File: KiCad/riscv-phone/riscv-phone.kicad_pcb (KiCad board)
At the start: 2 copper layers, 0 parts

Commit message: Initial microcontroller board
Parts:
- added C10: 12pF, Capacitor_SMD:C_0603_1608Metric, F.Cu at (134.7, 133.0)
- added C11: 0.1uF, Capacitor_SMD:C_0603_1608Metric, F.Cu at (128.8, 141.2)
- added C12: 0.1uF, Capacitor_SMD:C_0603_1608Metric, F.Cu at (144.1, 139.3)
- added C13: 0.1uF, Capacitor_SMD:C_0603_1608Metric, F.Cu at (138.2, 150.6)
- added C14: 0.1uF, Capacitor_SMD:C_0603_1608Metric, F.Cu at (135.6, 136.4)
- added C15: 0.1uF, Capacitor_SMD:C_0603_1608Metric, F.Cu at (146.3, 140.0)
- added C16: 1uF, Capacitor_SMD:C_0603_1608Metric, F.Cu at (141.9, 150.5)
- added C17: 1uF, Capacitor_SMD:C_0603_1608Metric, F.Cu at (132.8, 146.3)
- added C18: 0.1uF, Capacitor_SMD:C_0603_1608Metric, F.Cu at (126.7, 143.8)
- added C19: 0.1uF, Capacitor_SMD:C_0603_1608Metric, F.Cu at (143.1, 130.8)
- added C20: 1uF, Capacitor_SMD:C_0603_1608Metric, F.Cu at (143.1, 132.5)
- added C21: 0.1uF, Capacitor_SMD:C_0603_1608Metric, F.Cu at (157.2, 134.2)
- added C22: 0.1uF, Capacitor_SMD:C_0603_1608Metric, F.Cu at (137.3, 111.9)
- added C23: 12pF, Capacitor_SMD:C_0603_1608Metric, F.Cu at (130.6, 112.5)
- added C24: 4.7uF, Capacitor_SMD:C_0603_1608Metric, F.Cu at (129.0, 121.8)
- added C25: 4.7uF, Capacitor_SMD:C_0603_1608Metric, B.Cu at (136.5, 120.9)
- added C26: 4.7uF, Capacitor_SMD:C_0603_1608Metric, B.Cu at (136.5, 117.3)
- added C27: 12pF, Capacitor_SMD:C_0603_1608Metric, F.Cu at (124.7, 112.5)
- added C28: 0.1uF, Capacitor_SMD:C_0603_1608Metric, F.Cu at (127.4, 121.8)
- added C29: 0.1uF, Capacitor_SMD:C_0603_1608Metric, B.Cu at (135.0, 120.9)
- added C30: 0.1uF, Capacitor_SMD:C_0603_1608Metric, B.Cu at (135.0, 117.3)
- added C31: 0.1uF, Capacitor_SMD:C_0603_1608Metric, F.Cu at (141.7, 126.7)
- added C32: 0.1uF, Capacitor_SMD:C_0603_1608Metric, F.Cu at (145.2, 117.3)
- added C33: 0.1uF, Capacitor_SMD:C_0603_1608Metric, F.Cu at (137.9, 126.7)
- added C34: 0.1uF, Capacitor_SMD:C_0603_1608Metric, F.Cu at (145.2, 122.2)
- added C35: 0.1uF, Capacitor_SMD:C_0603_1608Metric, F.Cu at (133.4, 111.1)
- added C36: 0.1uF, Capacitor_SMD:C_0603_1608Metric, F.Cu at (142.5, 110.9)
- added C59: 0.1uF, Capacitor_SMD:C_0603_1608Metric, F.Cu at (158.4, 150.2)
- added C7: 10nF, Capacitor_SMD:C_0603_1608Metric, F.Cu at (126.0, 132.1)
- added C8: 0.1uF, Capacitor_SMD:C_0603_1608Metric, F.Cu at (156.2, 130.6)
- added C9: 12pF, Capacitor_SMD:C_0603_1608Metric, F.Cu at (140.7, 131.7)
- added C90: 1uF, Capacitor_SMD:C_0603_1608Metric, B.Cu at (122.9, 123.7)
- added C91: 1uF, Capacitor_SMD:C_0603_1608Metric, B.Cu at (126.6, 123.6)
- added C92: 1uF, Capacitor_SMD:C_0603_1608Metric, B.Cu at (126.6, 129.2)
- added C93: 1uF, Capacitor_SMD:C_0603_1608Metric, B.Cu at (123.4, 129.2)
- added D1: 1N4448W, Diode_SMD:D_SOD-123, F.Cu at (121.3, 132.5)
- added D2: BAT54L, Package_TO_SOT_SMD:SOT-23, F.Cu at (125.9, 129.2)
- added D3: BAT54L, Package_TO_SOT_SMD:SOT-23, F.Cu at (121.4, 142.5)
- added D4: SLEEP_LED, LED_SMD:LED_0805_2012Metric, F.Cu at (125.9, 150.4)
- added D5: D_TVS, LED_SMD:LED_0603_1608Metric_Pad1.05x0.95mm_HandSolder, F.Cu at (120.5, 126.1)
- added D8: D_TVS, LED_SMD:LED_0603_1608Metric_Pad1.05x0.95mm_HandSolder, F.Cu at (124.8, 120.4)
- added D9: D_TVS, LED_SMD:LED_0603_1608Metric_Pad1.05x0.95mm_HandSolder, F.Cu at (124.8, 117.1)
- added FB1: 600R, Inductor_SMD:L_0805_2012Metric_Pad1.15x1.40mm_HandSolder, B.Cu at (138.4, 121.0)
- added FB2: 600R, Inductor_SMD:L_0805_2012Metric_Pad1.15x1.40mm_HandSolder, B.Cu at (138.4, 117.2)
- added J1: USB_B_Micro, Connector_USB:USB_Micro-B_Molex-105017-0001, F.Cu at (120.9, 119.1)
- added J2: Conn_01x04, Connector_PinHeader_2.54mm:PinHeader_1x04_P2.54mm_Vertical, F.Cu at (119.6, 153.9)
- added J3: Conn_01x04, Connector_PinHeader_2.54mm:PinHeader_1x04_P2.54mm_Vertical, F.Cu at (153.4, 116.1)
- added J4: Conn_01x06, Connector_PinHeader_2.54mm:PinHeader_1x06_P2.54mm_Vertical, F.Cu at (148.3, 111.8)
- added J5: Conn_01x04, Connector_PinHeader_2.54mm:PinHeader_1x04_P2.54mm_Vertical, F.Cu at (161.3, 121.2)
- added J6: Conn_01x06, Connector_PinHeader_2.54mm:PinHeader_1x06_P2.54mm_Vertical, F.Cu at (161.3, 152.4)
- added J7: Conn_01x09, Connector_PinHeader_2.54mm:PinHeader_1x09_P2.54mm_Vertical, F.Cu at (124.7, 154.1)
- added J8: Conn_01x02, Connector_PinHeader_2.54mm:PinHeader_1x02_P2.54mm_Vertical, F.Cu at (121.7, 111.1)
- added Q1: Q_DUAL_NMOS_S1G1D2S2G2D1, Package_TO_SOT_SMD:SOT-363_SC-70-6, F.Cu at (126.7, 136.4)
- added Q2: IRLML6402, Package_TO_SOT_SMD:SOT-23, F.Cu at (119.5, 138.9)
- added R10: 100k, Resistor_SMD:R_0603_1608Metric, F.Cu at (123.7, 139.1)
- added R11: 4.7k, Resistor_SMD:R_0603_1608Metric, F.Cu at (123.8, 150.2)
- added R12: 100, Resistor_SMD:R_0603_1608Metric, F.Cu at (145.9, 128.1)
- added R23: 12k, Resistor_SMD:R_0603_1608Metric, F.Cu at (127.6, 117.3)
- added R24: 12k, Resistor_SMD:R_0603_1608Metric, F.Cu at (126.7, 125.2)
- added R25: 4.7k, Resistor_SMD:R_0603_1608Metric, F.Cu at (147.6, 114.8)
- added R26: 10k, Resistor_SMD:R_0603_1608Metric, F.Cu at (145.0, 113.8)
- added R27: 1k, Resistor_SMD:R_0603_1608Metric, F.Cu at (133.9, 129.5)
- added R28: 1k, Resistor_SMD:R_0603_1608Metric, F.Cu at (147.4, 118.9)
- added R29: 1k, Resistor_SMD:R_0603_1608Metric, F.Cu at (132.3, 127.3)
- added R30: 1k, Resistor_SMD:R_0603_1608Metric, F.Cu at (149.9, 120.9)
- added R34: 2.2k, Resistor_SMD:R_0603_1608Metric, F.Cu at (148.0, 149.5)
- added R35: 2.2k, Resistor_SMD:R_0603_1608Metric, F.Cu at (146.3, 149.5)
- added R53: 100k, Resistor_SMD:R_0603_1608Metric, F.Cu at (156.2, 126.5)
- added R54: 4.7k, Resistor_SMD:R_0603_1608Metric, F.Cu at (158.2, 145.9)
- added R6: 100k, Resistor_SMD:R_0603_1608Metric, F.Cu at (121.3, 134.7)
- added R7: 100k, Resistor_SMD:R_0603_1608Metric, F.Cu at (124.2, 126.1)
- added R8: 100k, Resistor_SMD:R_0603_1608Metric, F.Cu at (124.2, 142.2)
- added R9: 100k, Resistor_SMD:R_0603_1608Metric, F.Cu at (123.7, 146.6)
- added RST1: Reset, Button_Switch_SMD:SW_SPST_B3U-1000P-B, F.Cu at (121.3, 129.0)
- added U1: FE310-G000, Package_DFN_QFN:QFN-48-1EP_6x6mm_P0.4mm_EP4.66x4.66mm_ThermalVias, F.Cu at (138.8, 142.4)
- added U12: SC18IS600, Package_SO:TSSOP-16_4.4x5mm_P0.65mm, F.Cu at (153.2, 146.1)
- added U17: 74AHC1G08, Package_TO_SOT_SMD:SOT-23-5, F.Cu at (129.7, 148.2)
- added U18: M95256-WMN6P, Package_SO:SOIC-8_3.9x4.9mm_P1.27mm, F.Cu at (153.4, 152.9)
- added U2: IL25LP128, Package_SO:SOIJ-8_5.3x5.3mm_P1.27mm, F.Cu at (152.4, 128.9)
- added U5: 74CBTLV3257, Package_SO:TSSOP-16_4.4x5mm_P0.65mm, F.Cu at (153.5, 138.0)
- added U9: FT2232H, Package_QFP:LQFP-64_10x10mm_P0.5mm, F.Cu at (137.5, 119.3)
- added U90: TLV75533PDBV, Package_TO_SOT_SMD:SOT-23-5, B.Cu at (126.6, 126.4)
- added U91: TLV75518PDBV, Package_TO_SOT_SMD:SOT-23-5, B.Cu at (122.8, 126.4)
- added X1: SiT1533, riscv-phone:Crystal_SMD_2012-4Pin_2.0x1.2mm, F.Cu at (129.3, 144.0)
- added Y1: 16 MHz, Crystal:Crystal_SMD_3225-4Pin_3.2x2.5mm, F.Cu at (137.7, 132.3)
- added Y2: 12 MHz, Crystal:Crystal_SMD_3225-4Pin_3.2x2.5mm, F.Cu at (127.6, 112.5)
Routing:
- net +1V8: track 0.00 -> 216.0 mm, vias 0 -> 10
- net /Microcontroller/VDD_3V3_MOFF: track 0.00 -> 187.9 mm, vias 0 -> 12
- net +3V3: track 0.00 -> 184.8 mm, vias 0 -> 8
- net GND: track 0.00 -> 177.1 mm, vias 0 -> 33
- net /Program and Debug/VUSB: track 0.00 -> 66.3 mm, vias 0 -> 3
- net /RESET: track 0.00 -> 59.1 mm, vias 0 -> 8
- net /Microcontroller/RESET_N_1V8: track 0.00 -> 45.3 mm, vias 0 -> 3
- net /Microcontroller/DEBUG_RX: track 0.00 -> 40.1 mm, vias 0 -> 2
- net /Microcontroller/KEYPAD_INT: track 0.00 -> 37.1 mm, vias 0 -> 1
- net /Microcontroller/MOSI: track 0.00 -> 36.8 mm, vias 0 -> 4
- net /Program and Debug/VCORE_FT: track 0.00 -> 35.9 mm
- net /Microcontroller/SCK: track 0.00 -> 33.3 mm, vias 0 -> 4
- net /Microcontroller/MISO: track 0.00 -> 32.5 mm, vias 0 -> 4
- net /Microcontroller/DEBUG_TX: track 0.00 -> 31.0 mm, vias 0 -> 2
- net /Microcontroller/QSPI_CS: track 0.00 -> 27.3 mm
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- added copper zone on B.Cu, net GND
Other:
- board outline added: 46.5 x 47 mm
- net class Default: clearance 0.2 -> 0.1524; trace_width 0.25 -> 0.1524; via_dia 0.8 -> 0.6858; via_drill 0.4 -> 0.3302
- rule trace_clearance: 0.2 -> 0.1524
- rule trace_min: 0.2 -> 0.1524
- rule via_min_drill: 0.3 -> 0.254
- rule via_min_size: 0.4 -> 0.6858

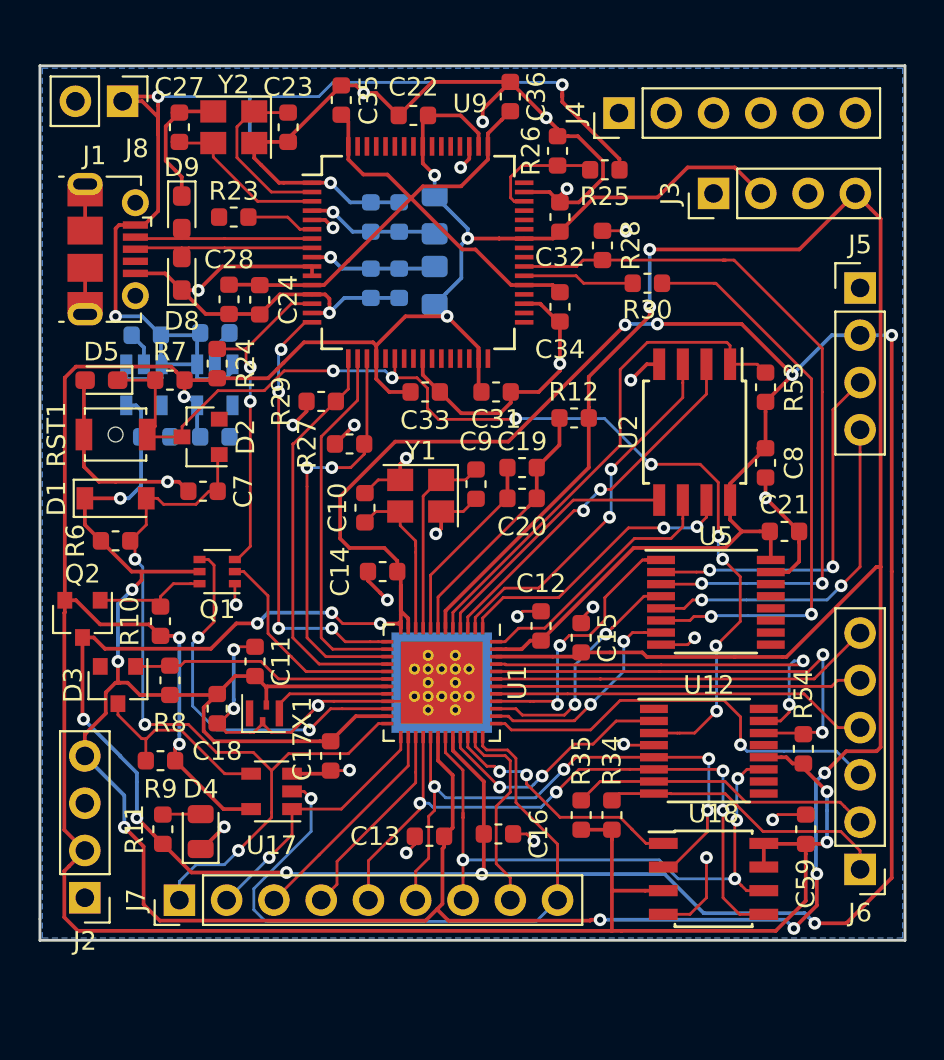
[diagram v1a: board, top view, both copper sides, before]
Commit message: added mounting holes, finalized layout
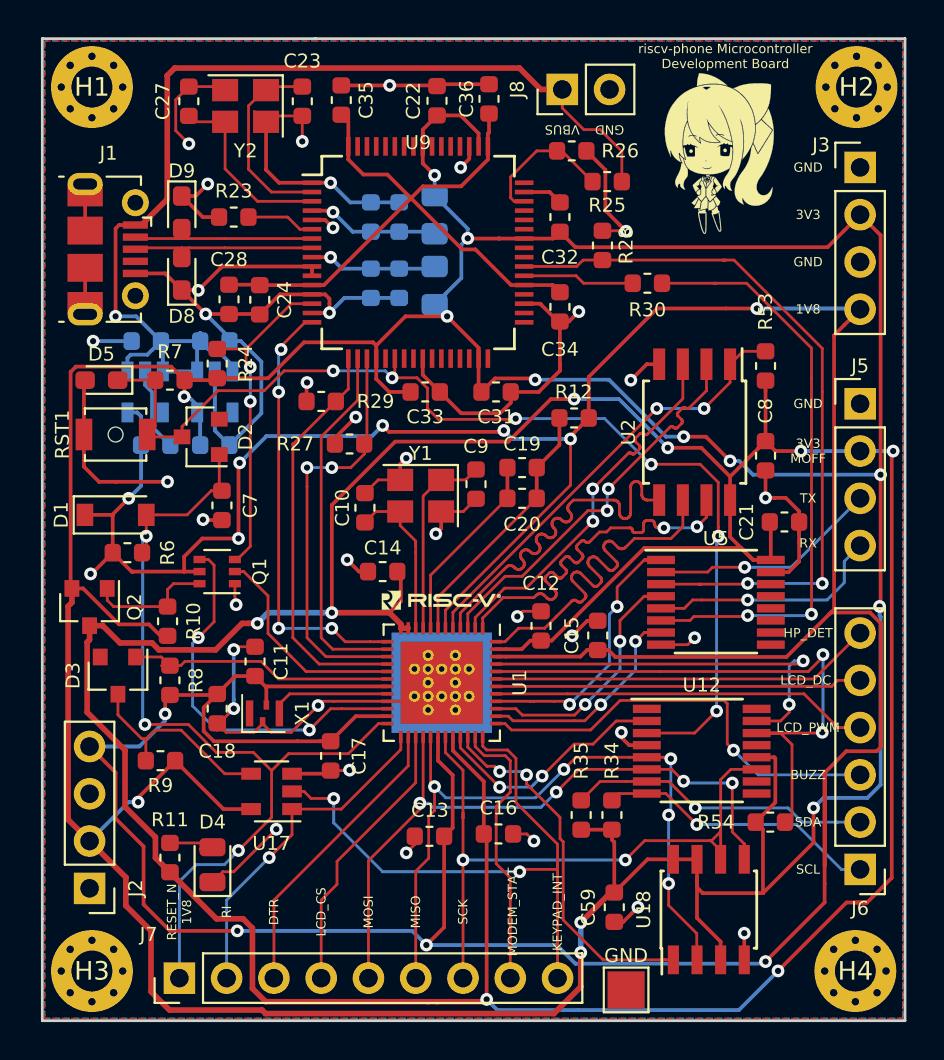
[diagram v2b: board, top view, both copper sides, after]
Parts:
- removed J4: Conn_01x06, Connector_PinHeader_2.54mm:PinHeader_1x06_P2.54mm_Vertical
- added G***: LOGO, riscv-phone:hidomi, B.Cu at (151.4, 119.6)
- added G***: LOGO, riscv-phone:riscv, F.Cu at (138.8, 137.9)
- added G***: LOGO, riscv-phone:copper_monika, F.Cu at (153.7, 113.8)
- added G***: LOGO, riscv-phone:copper_outline_4000dpi, F.Cu at (153.7, 113.8)
- added GND: TestPoint, TestPoint:TestPoint_Pad_2.0x2.0mm, F.Cu at (148.7, 158.9)
- added H1: MountingHole_Pad, MountingHole:MountingHole_2.2mm_M2_Pad_Via, F.Cu at (120.0, 110.4)
- added H2: MountingHole_Pad, MountingHole:MountingHole_2.2mm_M2_Pad_Via, F.Cu at (161.1, 110.4)
- added H3: MountingHole_Pad, MountingHole:MountingHole_2.2mm_M2_Pad_Via, F.Cu at (120.0, 157.9)
- added H4: MountingHole_Pad, MountingHole:MountingHole_2.2mm_M2_Pad_Via, F.Cu at (161.0, 157.9)
- moved J8 23.6 mm to (145.3, 110.5), turned to 90 degrees
- moved C59 11.1 mm to (148.1, 154.4), turned to 270 degrees
- moved J3 8.00 mm to (161.3, 114.7), turned to 0 degrees
- moved J5 6.22 mm to (161.3, 127.4)
- moved R54 4.32 mm to (156.5, 149.9), turned to 0 degrees
- moved J7 4.19 mm to (124.7, 158.2)
- moved D4 1.89 mm to (126.5, 152.1)
- moved U18 1.67 mm to (153.2, 154.6), turned to 90 degrees
- moved C23 1.59 mm to (131.3, 111.1)
- moved R11 1.57 mm to (124.2, 151.8)
- moved C22 1.49 mm to (138.6, 111.1), turned to 90 degrees
- moved C27 1.49 mm to (125.2, 111.1)
- moved Y2 1.31 mm to (128.3, 111.4)
- moved C7 1.27 mm to (127.0, 132.8), turned to 270 degrees
- moved C36 1.15 mm to (141.4, 111.0)
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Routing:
- net +3V3: track 184.8 -> 253.2 mm, vias 8 -> 13
- net +1V8: track 216.0 -> 232.0 mm, vias 10 -> 12
- net GND: track 177.1 -> 184.9 mm, vias 33 -> 36
- net /Microcontroller/MODEM_RX: track 19.9 -> 12.6 mm, vias 2 -> 1
- net /Microcontroller/QSPI_SCK: track 14.5 -> 21.2 mm
- net /Microcontroller/MISO: track 32.5 -> 39.0 mm, vias 4 -> 5
- net /Microcontroller/IO0: track 14.1 -> 20.4 mm
- net /Microcontroller/EEPROM_CS: track 13.5 -> 19.7 mm
- net /Microcontroller/MODEM_TX: track 19.0 -> 12.8 mm, vias 2 -> 1
- net /Microcontroller/BRIDGE_INT: track 25.4 -> 31.3 mm
- net /Microcontroller/IO3: track 16.3 -> 20.9 mm
- net /Microcontroller/KEYPAD_INT: track 37.1 -> 32.8 mm, vias 1 -> 2
- net /Microcontroller/RI: track 14.2 -> 18.4 mm
- net /Microcontroller/LCD_CS: track 10.9 -> 15.1 mm
- net /Microcontroller/MODEM_STATUS: track 11.6 -> 15.0 mm
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- added copper zone on F.Cu, net GND
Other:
- board size 46.5 x 47 mm -> 46.4 x 52.8 mm
- board text added: "1V8"
- board text added: "3V3"
- board text added: "3V3 MOFF"
- board text added: "BUZZ"
- board text added: "DTR"
- board text added: "GND"
- board text added: "HP_DET"
- board text added: "KEYPAD_INT"
- board text added: "LCD_CS"
- board text added: "LCD_DC"
- board text added: "LCD_PWM"
- board text added: "Layout: Spencer Moss"
- board text added: "MISO"
- board text added: "MODEM_STAT"
- board text added: "MOSI"
- board text added: "RESET_N 1V8"
- board text added: "RI"
- board text added: "RX"
- board text added: "SCK"
- board text added: "SCL"
- board text added: "SDA"
- board text added: "TX"
- board text added: "VBUS"
- board text added: "riscv-phone Microcontroller Development Board"

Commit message: Finalized pcb layout
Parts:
- removed GND: TestPoint, TestPoint:TestPoint_Pad_2.0x2.0mm
- removed J6: Conn_01x06, Connector_PinHeader_2.54mm:PinHeader_1x06_P2.54mm_Vertical
- removed J8: Conn_01x02, Connector_PinHeader_2.54mm:PinHeader_1x02_P2.54mm_Vertical
- added C60: 0.1uF, Capacitor_SMD:C_0603_1608Metric, F.Cu at (149.6, 151.0)
- added J4: Conn_01x11, Connector_PinHeader_2.54mm:PinHeader_1x11_P2.54mm_Vertical, F.Cu at (124.7, 158.2)
- added TP1: TestPoint, TestPoint:TestPoint_Pad_2.0x2.0mm, F.Cu at (161.6, 125.8)
- J5: value Conn_01x04 -> Conn_01x10; footprint Connector_PinHeader_2.54mm:PinHeader_1x04_P2.54mm_Vertical -> Connector_PinHeader_2.54mm:PinHeader_1x10_P2.54mm_Vertical
- J7: value Conn_01x09 -> Conn_01x02; footprint Connector_PinHeader_2.54mm:PinHeader_1x09_P2.54mm_Vertical -> Connector_PinHeader_2.54mm:PinHeader_1x02_P2.54mm_Vertical
- moved J7 52.0 mm to (145.3, 110.5)
- moved J5 24.8 mm to (161.3, 152.1), turned to 180 degrees
- moved G*** 8.64 mm to (138.8, 146.6)
- moved C59 4.76 mm to (151.4, 151.0), turned to 90 degrees
- moved R54 2.93 mm to (157.4, 147.1), turned to 90 degrees
- moved U18 1.94 mm to (155.1, 154.9)
- moved R34 1.65 mm to (147.3, 151.0)
- moved R35 1.65 mm to (145.7, 151.0)
- moved C13 1.37 mm to (139.1, 151.6), turned to 270 degrees
- moved G*** 1.08 mm to (150.4, 119.6)
- moved D4 0.90 mm to (127.4, 152.3), turned to 180 degrees
- moved C21 0.74 mm to (156.5, 133.5), turned to 90 degrees
- moved G*** 0.51 mm to (154.2, 113.8) (x2)
- moved U12 0.46 mm to (152.5, 146.4)
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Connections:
- net /SCL renamed /Microcontroller/SCL
- net /SDA renamed /Microcontroller/SDA
- D2 pad 3: /RESET -> /Microcontroller/RESET
- D5 pad 1: /RESET -> /Microcontroller/RESET
- J5 pad 1: GND -> /Microcontroller/MODEM_RST
- J5 pad 2: /Microcontroller/VDD_3V3_MOFF -> /Microcontroller/MODEM_STATUS
- J5 pad 3: /Microcontroller/MODEM_RX -> /Microcontroller/BUZZER
- J5 pad 4: /Microcontroller/MODEM_TX -> /Microcontroller/LCD_LED_PWM
- J7 pad 1: /Microcontroller/RESET_N_1V8 -> /Program and Debug/VUSB
- J7 pad 2: /Microcontroller/RI -> GND
- R7 pad 2: /RESET -> /Microcontroller/RESET
- RST1 pad 2: /RESET -> /Microcontroller/RESET
- U1 pad 25: /Microcontroller/RI -> /Microcontroller/KEYPAD_INT
- U1 pad 26: /Microcontroller/DTR -> /Microcontroller/RI
- U1 pad 33: /Microcontroller/BRIDGE_CS -> /Microcontroller/EEPROM_CS
- U1 pad 34: /Microcontroller/EEPROM_CS -> /Microcontroller/BRIDGE_CS
- U1 pad 35: /Microcontroller/MODEM_STATUS -> /Microcontroller/LCD_RST
- U1 pad 36: /Microcontroller/KEYPAD_INT -> /Microcontroller/DTR
- U12 pad 1: (no net) -> /Microcontroller/MODEM_STATUS
- U12 pad 3: /RESET -> /Microcontroller/RESET
- U12 pad 9: (no net) -> /Microcontroller/MODEM_RST
- U9 pad 22: /RESET -> (no net)
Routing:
- net /Microcontroller/RESET: track 0.00 -> 78.9 mm, vias 0 -> 7
- net /RESET: track 58.1 -> 0.00 mm, vias 6 -> 0
- net +1V8: track 232.0 -> 250.4 mm, vias 12 -> 16
- net /Microcontroller/LCD_RST: track 0.00 -> 15.0 mm
- net GND: track 184.9 -> 171.0 mm, vias 36 -> 34
- net /Microcontroller/KEYPAD_INT: track 32.8 -> 19.7 mm, vias 2 -> 0
- net /Microcontroller/MODEM_RST: track 0.00 -> 7.76 mm
- net /Microcontroller/BRIDGE_INT: track 31.3 -> 26.2 mm
- net +3V3: track 253.2 -> 258.1 mm, vias 13 -> 12
- net /Microcontroller/FT_RESET: track 20.4 -> 16.5 mm
- net /Microcontroller/EEPROM_CS: track 19.7 -> 23.5 mm
- net /Microcontroller/VDD_3V3_MOFF: track 191.3 -> 194.7 mm
- net /Microcontroller/BRIDGE_WAKEUP: track 21.5 -> 24.0 mm
- net /Microcontroller/SCL: track 15.4 -> 13.5 mm, vias 1 -> 0
- net /Microcontroller/MODEM_TX: track 12.8 -> 11.3 mm
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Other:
- board text added: "HP DET"
- board text added: "KEY INT"
- board text added: "LCD CS"
- board text added: "LCD DC"
- board text added: "LCD PWM"
- board text added: "LCD RST"
- board text added: "MDM RST"
- board text added: "MDM STAT"
- board text added: "RESET"
- board text removed: "HP_DET"
- board text removed: "KEYPAD_INT"
- board text removed: "LCD_CS"
- board text removed: "LCD_DC"
- board text removed: "LCD_PWM"
- board text removed: "MODEM_STAT"

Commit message: rev 1.1
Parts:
- removed the G*** at (154.2, 113.8) (x2)
- removed the G*** at (138.8, 146.6)
- added G***: LOGO, riscv-phone:monika_silk, F.Cu at (154.2, 113.8)
- added G***: LOGO, riscv-phone:riscv-big, F.Cu at (139.0, 146.6)
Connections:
- D2 pad 3: /Microcontroller/RESET -> /RESET
- D5 pad 1: /Microcontroller/RESET -> /RESET
- J5 pad 10: /Microcontroller/RESET -> /RESET
- R7 pad 2: /Microcontroller/RESET -> /RESET
- RST1 pad 2: /Microcontroller/RESET -> /RESET
- U12 pad 3: /Microcontroller/RESET -> /RESET
- U9 pad 22: (no net) -> /RESET
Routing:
- net /RESET: track 0.00 -> 79.8 mm, vias 0 -> 7
- net /Microcontroller/RESET: track 78.9 -> 0.00 mm, vias 7 -> 0
- net /Microcontroller/JTAG_TMS: track 22.4 -> 21.1 mm
- net /Microcontroller/VDD_3V3_MOFF: track 194.7 -> 195.6 mm
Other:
- board text added: "RISC-V Phone Microcontroller Board"
- board text added: "rev 1.1"
- board text removed: "riscv-phone Microcontroller Development Board"
